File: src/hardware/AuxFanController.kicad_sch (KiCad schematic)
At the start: 11 parts, among them U1 PIC12F1501, U2 MCP9701A

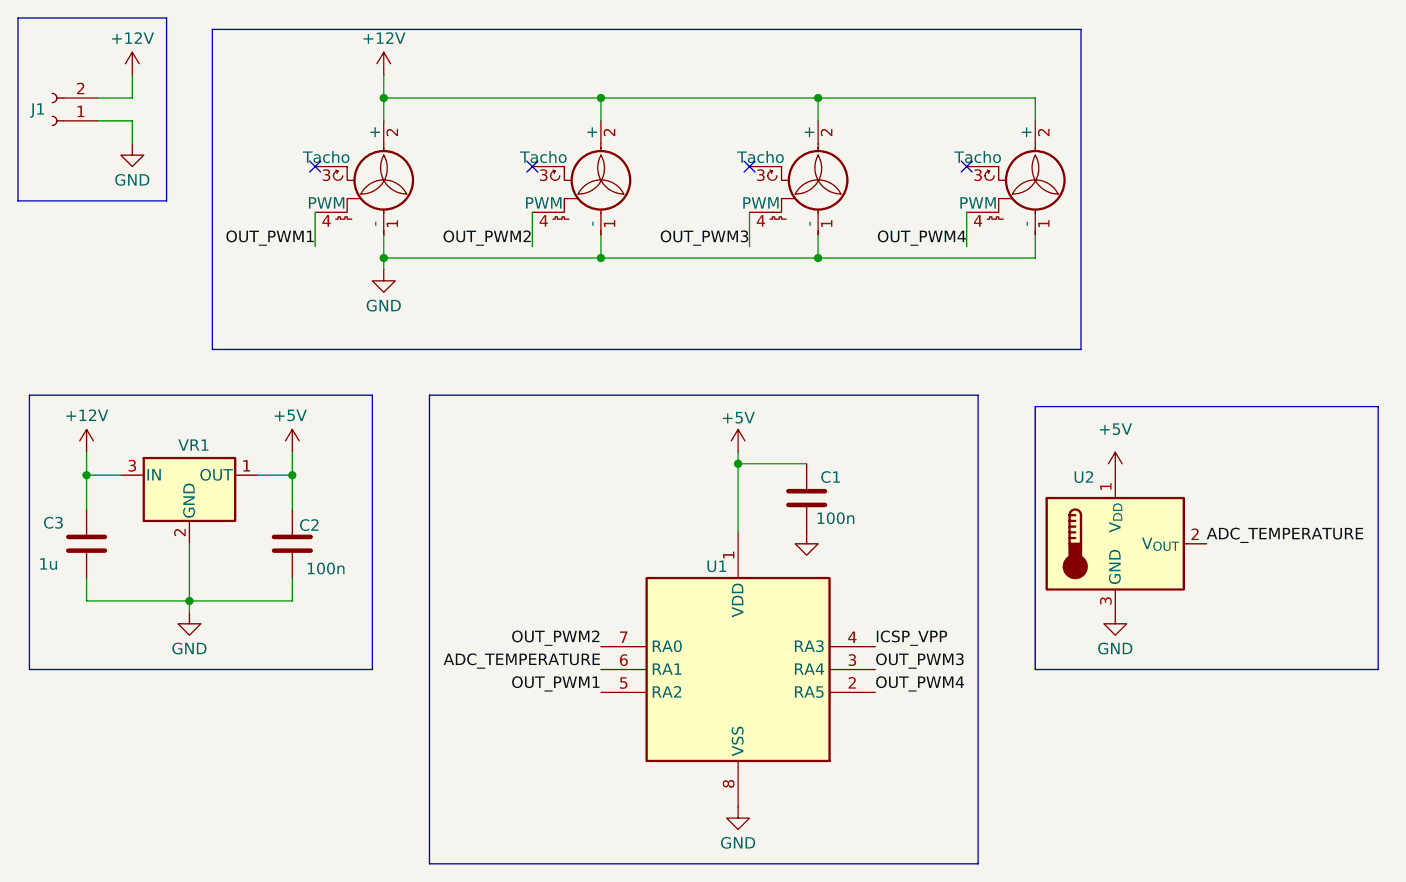
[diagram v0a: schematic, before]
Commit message: Refactoring to make board smaller
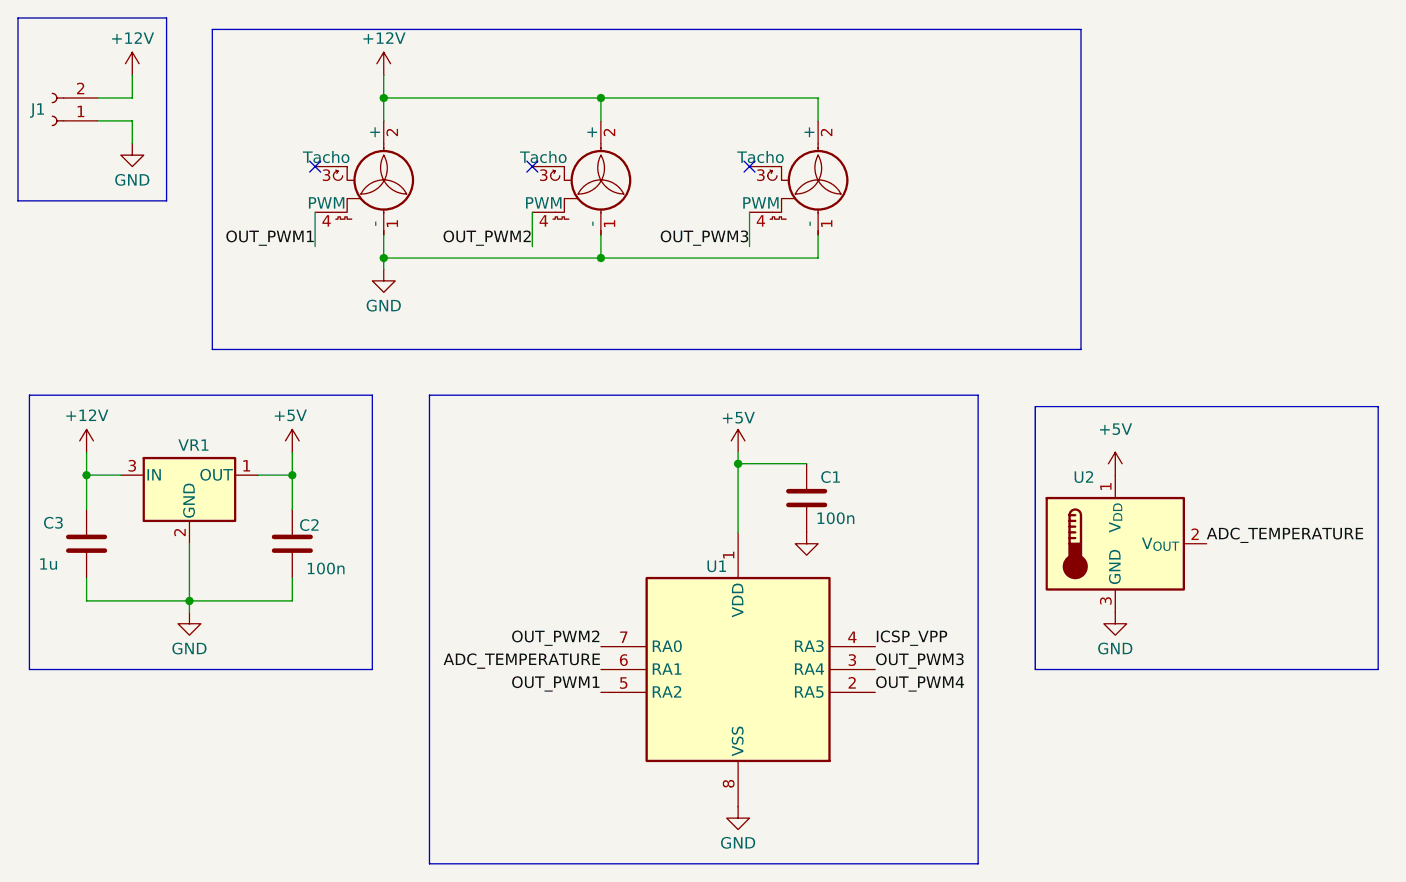
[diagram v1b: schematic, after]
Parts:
- removed J5: (no value), symbol Motor:Fan_4pin
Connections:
- no-connect marks 4 -> 3
